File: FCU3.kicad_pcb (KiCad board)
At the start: 4 copper layers, 36.7 x 36.7 mm, 93 parts, among them J1 SM06B-SRSS-TB_LF__SN_, J2 SM06B-SRSS-TB_LF__SN_, J3 UJ20-C-H-G-SMT-1-P16-TR, J4 SM08B-SRSS-TB_LF__SN_, J6 UJ20-C-H-G-SMT-1-P16-TR, Q2 SS8050, U1 MPU-6500, U2 NCV4274AST33T3G, U3 MCP1700x-330xxTT, U5 STM32F405RGTx, Y1 LFXTAL055207Bulk

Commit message: Layout Draft Complete
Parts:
- removed the C1 at (220.5, 81.2)
- removed the C1 at (140.7, 81.2)
- removed C10: 10uF, Capacitor_SMD:C_0603_1608Metric_Pad1.08x0.95mm_HandSolder
- removed the C11 at (212.4, 92.3)
- removed the C11 at (155.6, 90.0)
- removed C12, C13, C14, C4, C5, C6: 100nF, Capacitor_SMD:C_0603_1608Metric_Pad1.08x0.95mm_HandSolder
- removed C15, C16: 27pF, Capacitor_SMD:C_0603_1608Metric_Pad1.08x0.95mm_HandSolder
- removed the C18 at (219.6, 97.9)
- removed the C18 at (155.6, 91.6)
- removed the C19 at (212.4, 95.7)
- removed the C19 at (141.1, 85.4)
- removed the C20 at (220.5, 84.6)
- removed the C20 at (143.4, 85.4)
- removed the C21 at (212.4, 99.0)
- removed the C21 at (145.8, 85.4)
- removed the C22 at (202.8, 102.9)
- removed the C22 at (148.2, 85.4)
- removed the C23 at (202.8, 104.9)
- removed the C23 at (150.7, 85.4)
- removed C32, C33: 27pF, Capacitor_SMD:C_0603_1608Metric
- removed C7, C8, C9: 2.2uF, Capacitor_SMD:C_0603_1608Metric_Pad1.08x0.95mm_HandSolder
- removed the D1 at (137.7, 82.3)
- removed the D1 at (213.7, 81.8)
- removed the H1 at (132.4, 74.5)
- removed the H1 at (188.7, 74.9)
- removed the H2 at (188.7, 82.0)
- removed the H2 at (162.9, 74.5)
- removed the H3 at (188.7, 89.2)
- removed the H3 at (162.9, 105.0)
- removed the H4 at (132.4, 105.0)
- removed the H4 at (188.7, 96.3)
- removed J2: SM06B-SRSS-TB_LF__SN_, KSE_connector:JST_SM06B-SRSS-TB_LF__SN_
- removed J6: UJ20-C-H-G-SMT-1-P16-TR, KSE_connector:SAMESKY_UJ20-C-H-G-SMT-1-P16-TR
- removed the JP3 at (197.3, 83.1)
- removed the JP3 at (149.9, 105.5)
- removed the PS1 at (218.5, 93.9)
- removed the PS1 at (154.2, 86.5)
- removed Q2: SS8050, Package_TO_SOT_SMD:SOT-23
- removed R10: 4.7k, Resistor_SMD:R_0603_1608Metric_Pad0.98x0.95mm_HandSolder
- removed the R11 at (193.7, 82.3)
- removed the R11 at (150.1, 88.6)
- removed R15, R9: 5.1k, Resistor_SMD:R_0805_2012Metric_Pad1.20x1.40mm_HandSolder
- removed the R5 at (216.7, 97.9)
- removed the R5 at (152.8, 90.9)
- removed the R6 at (216.7, 99.9)
- removed the R6 at (150.1, 90.2)
- removed the R8 at (190.5, 108.8)
- removed the R8 at (155.1, 72.2)
- removed the U1 at (198.8, 104.6)
- removed the U1 at (160.8, 98.7)
- removed U5: STM32F405RGTx, Package_QFP:LQFP-64_10x10mm_P0.5mm
- added C1: 1uF, Capacitor_SMD:C_0402_1005Metric, F.Cu at (154.3, 68.6)
- added C11: 22uF, Capacitor_SMD:C_1206_3216Metric, F.Cu at (164.2, 90.5)
- added C18: 100nF, Capacitor_SMD:C_0402_1005Metric, F.Cu at (162.6, 89.4)
- added C19: 22uF, Capacitor_SMD:C_1206_3216Metric, F.Cu at (158.1, 83.9)
- added C20: 1uF, Capacitor_SMD:C_0402_1005Metric, F.Cu at (154.3, 71.7)
- added C21: 22uF, Capacitor_SMD:C_1206_3216Metric, F.Cu at (158.1, 86.3)
- added C22: 100nF, Capacitor_SMD:C_0402_1005Metric, F.Cu at (147.4, 81.5)
- added C23: 100nF, Capacitor_SMD:C_0402_1005Metric, F.Cu at (151.2, 84.9)
- added D1: SS14-M3/5AT, Diode_SMD:D_SMA, F.Cu at (148.4, 70.6)
- added D4: LED Green, Diode_SMD:D_0603_1608Metric, F.Cu at (147.8, 102.1)
- added H1: MountingHole_Pad_MP, MountingHole:MountingHole_3.2mm_M3_DIN965_Pad, F.Cu at (132.8, 70.1)
- added H2: MountingHole_Pad_MP, MountingHole:MountingHole_3.2mm_M3_DIN965_Pad, F.Cu at (162.4, 70.0)
- added H3: MountingHole_Pad_MP, MountingHole:MountingHole_3.2mm_M3_DIN965_Pad, F.Cu at (131.9, 100.5)
- added H4: MountingHole_Pad_MP, MountingHole:MountingHole_3.2mm_M3_DIN965_Pad, F.Cu at (162.4, 100.5)
- added J5: SM06B-SRSS-TB(LF)(SN), KSE_connector:JST_SM06B-SRSS-TB(LF)(SN), F.Cu at (160.4, 78.0)
- added JP3: SolderJumper_2_Bridged, Jumper:SolderJumper-2_P1.3mm_Bridged2Bar_Pad1.0x1.5mm, B.Cu at (143.1, 102.4)
- added PS1: TPSM84338RCJR, KSE_DCDC:TPSM84338RCJR, F.Cu at (159.2, 89.7)
- added Q1: SS8050, Package_TO_SOT_SMD:SOT-23, F.Cu at (156.9, 96.2)
- added R11: 10k, Resistor_SMD:R_0402_1005Metric, F.Cu at (158.4, 94.6)
- added R5: 10k, Resistor_SMD:R_0402_1005Metric, F.Cu at (162.6, 87.4)
- added R6: 140k, Resistor_SMD:R_0402_1005Metric, F.Cu at (160.9, 86.5)
- added R8: 10k, Resistor_SMD:R_0402_1005Metric, F.Cu at (154.2, 98.2)
- added U1: MPU-6500, KSE_sensor:QFN40P300X300X95-25N, F.Cu at (147.3, 84.2)
- C17: footprint Capacitor_SMD:C_0603_1608Metric_Pad1.08x0.95mm_HandSolder -> Capacitor_SMD:C_0402_1005Metric
- C2: value 1uF -> 18pF; footprint Capacitor_SMD:C_0603_1608Metric_Pad1.08x0.95mm_HandSolder -> Capacitor_SMD:C_0603_1608Metric; moved to F.Cu
- C3: value 100nF -> 18pF; footprint Capacitor_SMD:C_0603_1608Metric_Pad1.08x0.95mm_HandSolder -> Capacitor_SMD:C_0603_1608Metric
- D2: value SS14 -> LED Red; footprint Diode_SMD:D_SMA -> Diode_SMD:D_0603_1608Metric
- J1: value SM06B-SRSS-TB_LF__SN_ -> SM06B-SRSS-TB(LF)(SN); footprint KSE_connector:JST_SM06B-SRSS-TB_LF__SN_ -> KSE_connector:JST_SM06B-SRSS-TB(LF)(SN)
- J4: value SM08B-SRSS-TB_LF__SN_ -> SM08B-SRSS-TB(LF)(SN); footprint KSE_connector:JST_SM08B-SRSS-TB_LF__SN_ -> KSE_connector:JST_SM08B-SRSS-TB(LF)(SN)
- R1: value 75k -> 4.7k; footprint Resistor_SMD:R_0603_1608Metric_Pad0.98x0.95mm_HandSolder -> Resistor_SMD:R_0402_1005Metric; moved to F.Cu
- R2, R3: value 10k -> 4.7k; footprint Resistor_SMD:R_0603_1608Metric_Pad0.98x0.95mm_HandSolder -> Resistor_SMD:R_0402_1005Metric; moved to F.Cu
- R4: value 1k -> 680; footprint Resistor_SMD:R_0603_1608Metric_Pad0.98x0.95mm_HandSolder -> Resistor_SMD:R_0402_1005Metric; moved to F.Cu
- R7: value 4.7k -> 680; footprint Resistor_SMD:R_0603_1608Metric_Pad0.98x0.95mm_HandSolder -> Resistor_SMD:R_0402_1005Metric; moved to F.Cu
- S1: value TS32-7-35-BK-B-260-RA-SMT-TR -> NO
- U2: value NCV4274AST33T3G -> AP7375-33SA-7; footprint KSE_DCDC:SOT230P700X175-4N -> KSE_DCDC:AP7375-33SA-7_DIO
- U3: value MCP1700x-330xxTT -> STM32F405RGT6; footprint Package_TO_SOT_SMD:SOT-23 -> Package_QFP:LQFP-64_10x10mm_P0.5mm; moved to F.Cu
- Y1: value LFXTAL055207Bulk -> 12MHz; footprint KSE_passive:Crystal_HC49-4H_Vertical -> KSE_passive:Crystal_SMD_Abracon_ABM8AIG-4Pin_3.2x2.5mm; moved to F.Cu
- moved R17 63.1 mm to (132.5, 74.5)
- moved R16 62.4 mm to (132.5, 75.6)
- moved D3 58.6 mm to (157.2, 70.6), turned to -90 degrees
- moved R14 58.3 mm to (135.8, 79.8)
- moved J3 58.3 mm to (141.2, 66.8), turned to 180 degrees
- moved R13 56.2 mm to (137.7, 79.8)
- moved C34 55.4 mm to (137.5, 98.7), turned to -90 degrees
- moved R12 55.1 mm to (163.7, 87.1), turned to -90 degrees
- moved C29 53.8 mm to (139.6, 86.3), turned to 180 degrees
- moved C27 53.6 mm to (136.1, 97.0), turned to 90 degrees
- moved C26 52.0 mm to (138.2, 87.7), turned to 180 degrees
- moved U2 51.8 mm to (152.8, 70.1), turned to -90 degrees
- moved C31 47.0 mm to (145.3, 101.7), turned to 180 degrees
- moved C28 44.2 mm to (145.3, 100.7), turned to 180 degrees
- moved C30 43.7 mm to (150.6, 89.8), turned to 90 degrees
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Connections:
- C2 pad 1: +3V3 -> /Project Architecture/Microcontroller/CLK_OUT
- C29 pad 1: Net-(U5-VCAP_2) -> Net-(U3-VCAP_2)
- C30 pad 1: Net-(U5-VCAP_1) -> Net-(U3-VCAP_1)
- D2 pad 1: Net-(D1-K) -> DGND
- D2 pad 2: /(lib_symbols/V_USB -> Net-(D2-A)
- D3 pad 2: /Project Architecture/Power/10–26V to 9V2A Step-Down Converter/+9V -> +9V
- J1 pad 1: +9V -> /Project Architecture/UART5_RX
- J1 pad 2: PGND -> /Project Architecture/UART5_TX
- J1 pad 3: /Project Architecture/UART4_TX -> DGND
- J1 pad 4: /Project Architecture/UART4_RX -> +3V3
- J1 pad 5: DGND -> /Project Architecture/I2C1_SCL
- J1 pad 6: /Project Architecture/SBUS_TX -> /Project Architecture/I2C1_SDA
- J4 pad 3: /(lib_symbols/ESC_SIG_M1 -> /Project Architecture/ESC_SIG_M1
- J4 pad 4: /(lib_symbols/ESC_SIG_M2 -> /Project Architecture/ESC_SIG_M2
- J4 pad 5: /(lib_symbols/ESC_SIG_M4 -> /Project Architecture/ESC_SIG_M4
- J4 pad 6: /(lib_symbols/ESC_SIG_M3 -> /Project Architecture/ESC_SIG_M3
- J4 pad 7: /(lib_symbols/ANA_ADC_CURR -> /Project Architecture/ANA_ADC_CURR
- J4 pad 8: /(lib_symbols/UART1_RX -> /Project Architecture/UART1_RX
- R1 pad 1: /(lib_symbols/ANA_ADC_VBAT -> +3V3
- R1 pad 2: +VBAT -> /Project Architecture/I2C1_SDA
- R2 pad 1: AGND -> +3V3
- R2 pad 2: /(lib_symbols/ANA_ADC_VBAT -> /Project Architecture/I2C1_SCL
- R3 pad 1: +3V3 -> /Project Architecture/SBUS_TX
- R3 pad 2: /(lib_symbols/UART2_RX -> Net-(Q1-B)
- R4 pad 1: Net-(Q2-B) -> /Project Architecture/Microcontroller/LED1
- R4 pad 2: /Project Architecture/SBUS_TX -> Net-(D2-A)
- R7 pad 1: /Project Architecture/I2C1_SCL -> /Project Architecture/Microcontroller/LED0
- R7 pad 2: +3V3 -> Net-(D4-A)
- S1 pad 1: /Project Architecture/Microcontroller/DFU_Enable -> +3V3
- S1 pad 2: +3V3 -> /Project Architecture/Microcontroller/DFU_Enable
- S1 pad SH1: (no net) -> DGND
- S1 pad SH2: (no net) -> DGND
- U2 pad 2: DGND -> +3V3
- U2 pad 3: +3V3 -> DGND
- U3 pad 1: DGND -> unconnected-(U3-VBAT-Pad1)
- U3 pad 2: +3V3 -> unconnected-(U3-PC13-Pad2)
- U3 pad 3: Net-(D1-K) -> unconnected-(U3-PC14-Pad3)
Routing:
- net +3V3: track 147.8 -> 72.0 mm, vias 11 -> 13
- net PGND: track 92.4 -> 41.5 mm, vias 11 -> 8
- net /(lib_symbols/Microcontroller/DFU_Enable: track 41.9 -> 0.00 mm, vias 4 -> 0
- net /(lib_symbols/UART2_RX: track 32.1 -> 0.00 mm, vias 3 -> 0
- net /Project Architecture/I2C1_SDA: track 41.2 -> 10.1 mm, vias 3 -> 2
- net /Project Architecture/I2C1_SCL: track 38.2 -> 8.11 mm, vias 4 -> 0
- net /Project Architecture/ANA_ADC_VBAT: track 0.00 -> 26.2 mm, vias 0 -> 2
- net +9V: track 54.1 -> 27.9 mm, vias 12 -> 1
- net /(lib_symbols/ANA_ADC_VBAT: track 26.0 -> 0.00 mm, vias 1 -> 0
- net /Project Architecture/ANA_ADC_CURR: track 0.00 -> 25.0 mm, vias 0 -> 2
- net /Project Architecture/UART5_TX: track 27.4 -> 4.21 mm, vias 3 -> 0
- net /Project Architecture/ESC_SIG_M1: track 0.00 -> 22.5 mm, vias 0 -> 2
- net /Project Architecture/Microcontroller/DFU_Enable: track 0.00 -> 22.3 mm
- net /(lib_symbols/ESC_SIG_M3: track 22.1 -> 0.00 mm, vias 2 -> 0
- net /Project Architecture/SBUS_TX: track 5.49 -> 27.2 mm, vias 1 -> 2
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- added copper zone on In2.Cu, net +3V3
- added copper zone on In1.Cu, net PGND
- removed copper zone on B.Cu, net +9V
- removed copper zone on In2.Cu, net +9V
- removed copper zone on B.Cu, net PGND
- removed copper zone on In2.Cu, net PGND
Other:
- board size 36.7 x 36.7 mm -> 37 x 37 mm
- board text added: "9V to 3.3V LDO Layout"
- board text added: "IMU Layout"
- board text added: "MCU Layout"
- board text added: "SBUS Inverter Layout"

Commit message: DRC/ERC Remaining
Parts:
- added J2: ST-LINK_Header, Connector_PinHeader_1.27mm:PinHeader_2x03_P1.27mm_Vertical_SMD, B.Cu at (148.7, 71.8)
- moved R3 3.01 mm to (154.0, 94.9)
- moved R11 3.01 mm to (155.5, 95.6)
- moved Q1 3.01 mm to (154.1, 97.1)
- moved R8 2.55 mm to (151.6, 98.2)
- moved R13 2.24 mm to (135.8, 78.8), turned to 180 degrees
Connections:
- R4 pad 1: /Project Architecture/Microcontroller/LED1 -> /Project Architecture/LED1
- R7 pad 1: /Project Architecture/Microcontroller/LED0 -> /Project Architecture/LED0
- U3 pad 46: /Project Architecture/Microcontroller/LED0 -> /Project Architecture/Microcontroller/SWDIO
- U3 pad 49: /Project Architecture/Microcontroller/LED1 -> /Project Architecture/Microcontroller/SWCLK
- U3 pad 55: unconnected-(U3-PB3-Pad55) -> /Project Architecture/Microcontroller/SWO
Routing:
- net /Project Architecture/Microcontroller/SWO: track 0.00 -> 31.2 mm, vias 0 -> 3
- net /Project Architecture/Microcontroller/SWDIO: track 0.00 -> 30.0 mm, vias 0 -> 3
- net /Project Architecture/Microcontroller/SWCLK: track 0.00 -> 25.9 mm, vias 0 -> 2
- net /Project Architecture/DIG_IMU_EXTI: track 1.80 -> 17.5 mm
- net /Project Architecture/SPI1_SCK: track 20.6 -> 33.8 mm, vias 2 -> 3
- net +9V: track 27.9 -> 40.5 mm
- net /Project Architecture/DIG_IMU_CS: track 5.87 -> 18.4 mm
- net +3V3: track 72.0 -> 83.5 mm, vias 13 -> 14
- net /Project Architecture/SPI1_SDO: track 3.16 -> 12.1 mm
- net AGND: track 34.1 -> 38.6 mm
- net DGND: track 80.6 -> 85.0 mm, vias 21 -> 22
- net /Project Architecture/SBUS_TX: track 27.2 -> 30.1 mm
- net /Project Architecture/UART4_RX: track 32.6 -> 35.2 mm
- net /Project Architecture/Microcontroller/LED1: track 2.25 -> 0.00 mm, vias 2 -> 0
- net /Project Architecture/UART2_RX: track 13.5 -> 11.4 mm
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- added copper zone on B.Cu, net +9V

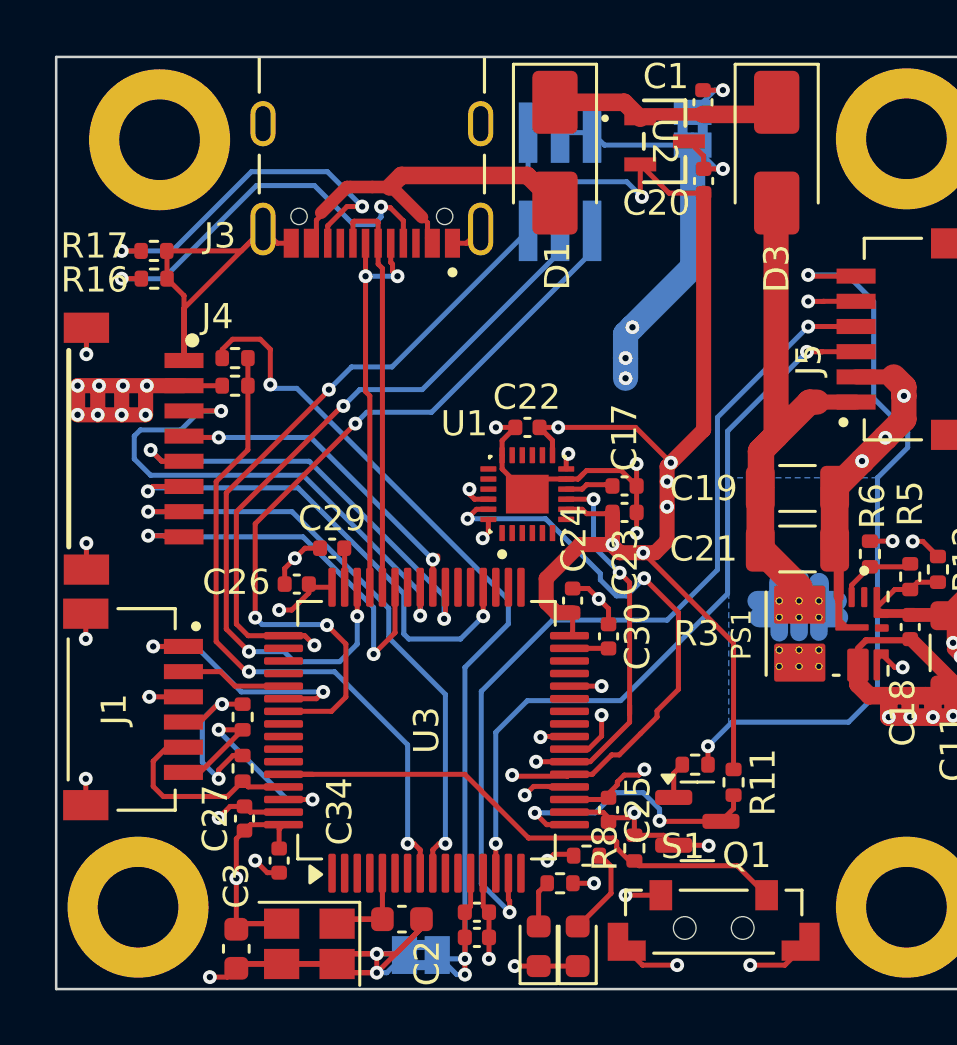
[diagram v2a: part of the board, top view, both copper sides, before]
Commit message: Added debugger pads, needs to fix LED
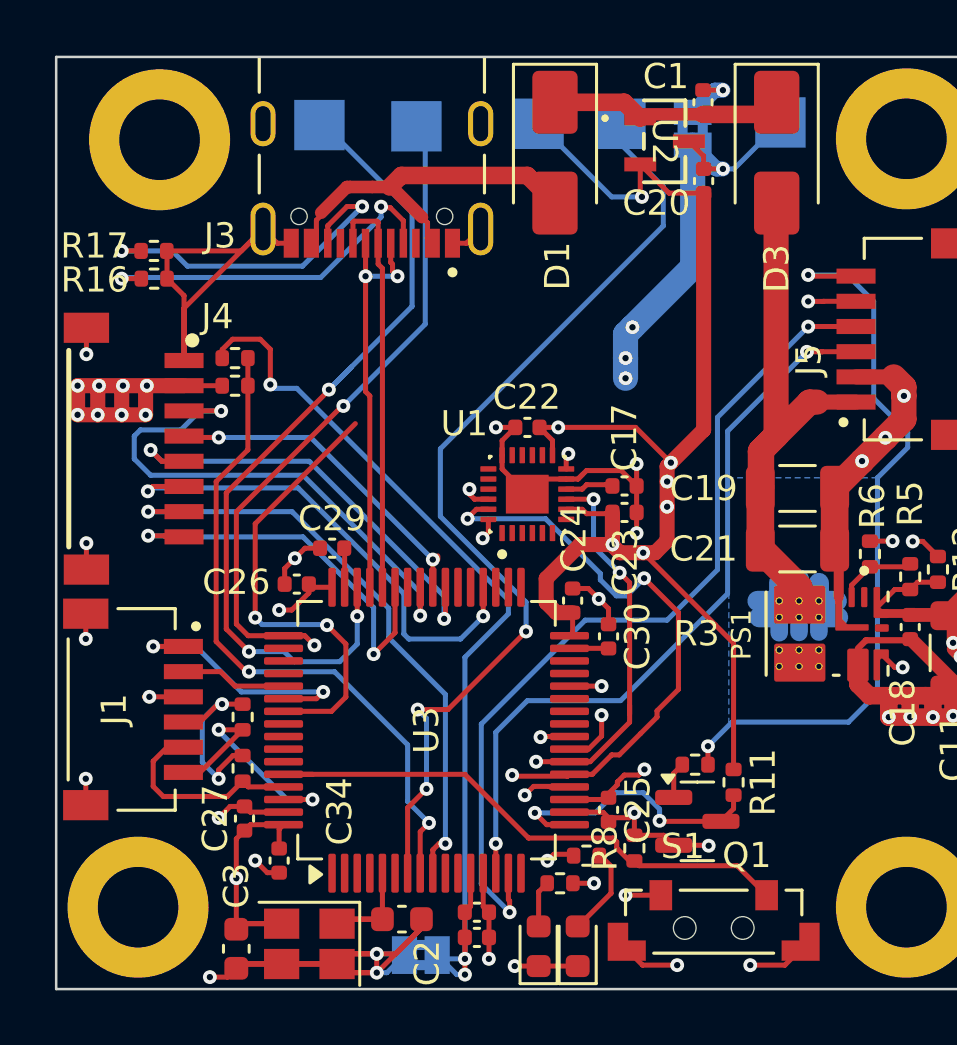
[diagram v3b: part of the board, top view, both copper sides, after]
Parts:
- removed J2: ST-LINK_Header, Connector_PinHeader_1.27mm:PinHeader_2x03_P1.27mm_Vertical_SMD
- added TP1: VCC, TestPoint:TestPoint_Pad_2.0x2.0mm, B.Cu at (147.8, 69.5)
- added TP2: SWDIO, TestPoint:TestPoint_Pad_2.0x2.0mm, B.Cu at (139.1, 69.5)
- added TP3: SWCLK, TestPoint:TestPoint_Pad_2.0x2.0mm, B.Cu at (142.9, 69.5)
- added TP4: GND, TestPoint:TestPoint_Pad_2.0x2.0mm, B.Cu at (157.4, 69.4)
- added TP5: RESET, TestPoint:TestPoint_Pad_2.0x2.0mm, B.Cu at (151.1, 69.5)
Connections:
- U3 pad 55: /Project Architecture/Microcontroller/SWO -> unconnected-(U3-PB3-Pad55)
- U3 pad 7: unconnected-(U3-NRST-Pad7) -> Net-(U3-NRST)
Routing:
- net Net-(U3-NRST): track 0.00 -> 38.5 mm, vias 0 -> 3
- net /Project Architecture/Microcontroller/SWO: track 31.2 -> 0.00 mm, vias 3 -> 0
- net unconnected-(U3-PB3-Pad55): track 0.00 -> 18.2 mm, vias 0 -> 2
- net /Project Architecture/Microcontroller/SWDIO: track 30.0 -> 34.3 mm
- net DGND: track 85.0 -> 82.6 mm
- net /Project Architecture/USB_CC1: track 16.0 -> 14.7 mm
- net +3V3: track 83.5 -> 82.3 mm
- net /Project Architecture/Microcontroller/SWCLK: track 25.9 -> 26.8 mm
- net /Project Architecture/UART4_RX: track 35.2 -> 34.5 mm
- net /Project Architecture/USB_CC2: track 14.7 -> 14.0 mm
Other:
- board text added: "CLK"
- board text added: "DIO"
- board text added: "GND"
- board text added: "RST"
- board text added: "VCC"

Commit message: Finished DRC/ERC
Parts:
- moved R7 7.97 mm to (151.1, 92.0), turned to 0 degrees
- moved R4 5.61 mm to (151.1, 93.0)
- moved D4 1.65 mm to (149.4, 102.1)
- moved D2 1.60 mm to (147.8, 102.1)
- moved H1 0.75 mm to (132.0, 70.1)
- moved R6 0.53 mm to (160.9, 86.0)
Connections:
- C11 pad 1: /Project Architecture/Power/VBAT -> +VBAT
- C18 pad 1: /Project Architecture/Power/VBAT -> +VBAT
- J1 pad MP: (no net) -> PGND
- J4 pad MP: (no net) -> PGND
- J5 pad MP: (no net) -> PGND
- PS1 pad 6: /Project Architecture/Power/VBAT -> +VBAT
- R4 pad 1: /Project Architecture/LED1 -> /Project Architecture/Microcontroller/LED1
- R7 pad 1: /Project Architecture/LED0 -> /Project Architecture/Microcontroller/LED0
- U3 pad 26: unconnected-(U3-PB0-Pad26) -> /Project Architecture/Microcontroller/LED1
- U3 pad 27: unconnected-(U3-PB1-Pad27) -> /Project Architecture/Microcontroller/LED0
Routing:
- net PGND: track 41.5 -> 75.7 mm, vias 8 -> 12
- net unconnected-(U3-PB3-Pad55): track 18.2 -> 0.00 mm, vias 2 -> 0
- net /Project Architecture/Power/VBAT: track 16.5 -> 0.00 mm, vias 4 -> 0
- net +VBAT: track 13.3 -> 26.9 mm, vias 8 -> 10
- net Net-(D4-A): track 1.85 -> 13.5 mm, vias 0 -> 2
- net Net-(D2-A): track 3.65 -> 13.1 mm, vias 0 -> 2
- net (no net): track 4.15 -> 0.00 mm, vias 4 -> 0
- net /Project Architecture/DIG_IMU_EXTI: track 17.5 -> 13.5 mm
- net /Project Architecture/SPI1_SDI: track 15.2 -> 17.8 mm, vias 3 -> 2
- net /Project Architecture/Microcontroller/LED1: track 0.00 -> 1.63 mm
- net /Project Architecture/Microcontroller/LED0: track 0.00 -> 1.63 mm
- net /Project Architecture/SPI1_SCK: track 33.8 -> 35.4 mm
- net /Project Architecture/Microcontroller/SWCLK: track 26.8 -> 25.5 mm, vias 2 -> 1
- net +9V: track 40.5 -> 39.2 mm
- net /Project Architecture/Microcontroller/SWDIO: track 34.3 -> 33.0 mm
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
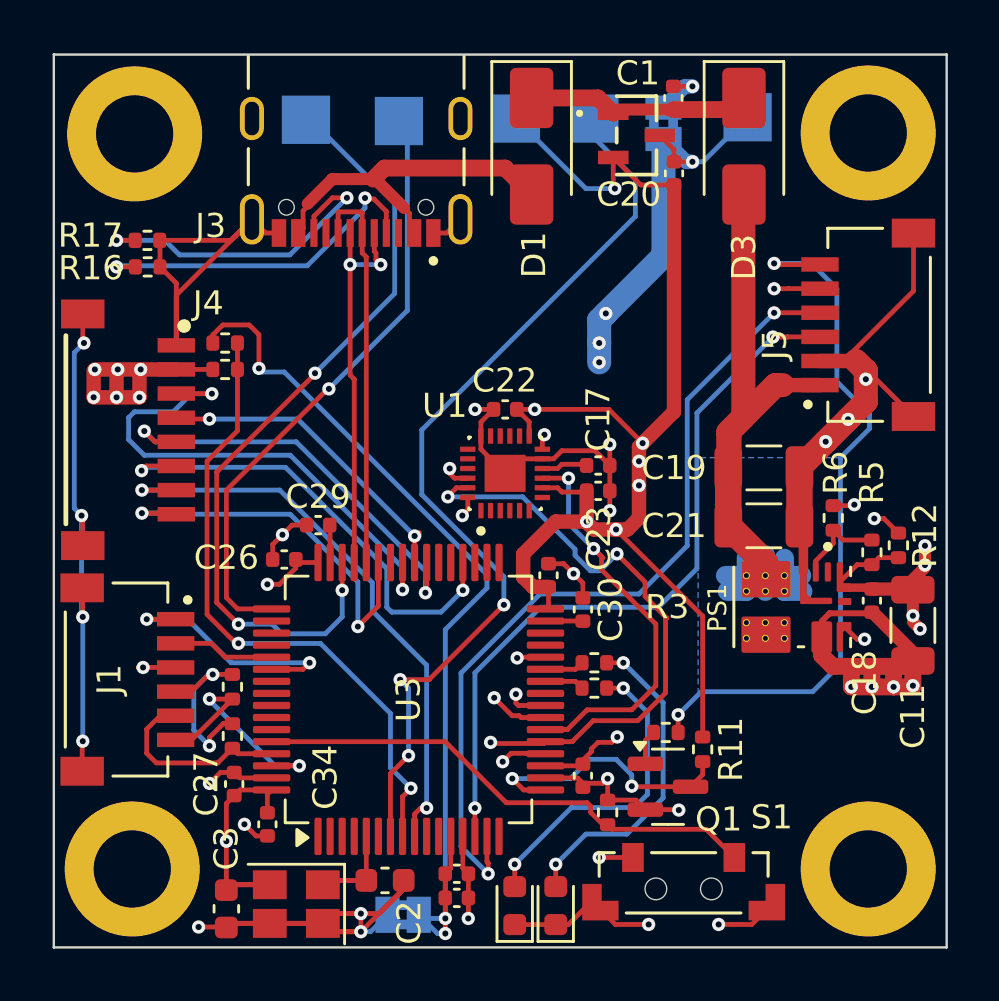
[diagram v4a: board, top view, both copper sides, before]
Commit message: Fixed ESC connector pinout
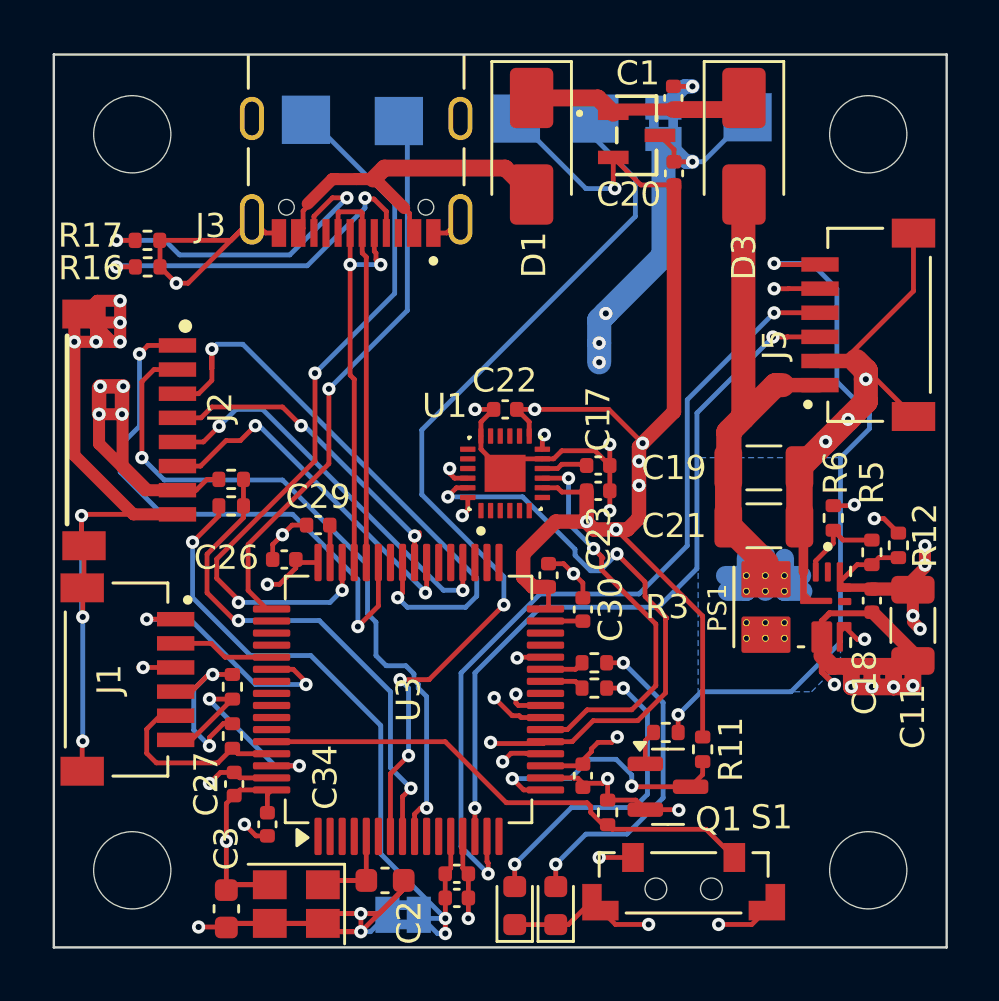
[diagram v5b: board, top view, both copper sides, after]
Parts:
- removed J4: SM08B-SRSS-TB(LF)(SN), KSE_connector:JST_SM08B-SRSS-TB(LF)(SN)
- added J2: SM08B-SRSS-TB(LF)(SN), KSE_connector:JST_SM08B-SRSS-TB(LF)(SN), F.Cu at (129.0, 82.3)
- H1, H2, H3, H4: value MountingHole_Pad_MP -> MountingHole; footprint MountingHole:MountingHole_3.2mm_M3_DIN965_Pad -> MountingHole:MountingHole_3.2mm_M3_ISO7380
- moved R13 6.75 mm to (136.0, 85.5)
- moved R14 4.56 mm to (136.0, 84.4)
- moved H1 0.10 mm to (131.9, 70.1)
- moved H2 0.05 mm to (162.4, 70.1)
- moved H3 0.05 mm to (131.9, 100.6)
- moved H4 0.05 mm to (162.4, 100.6)
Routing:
- net +VBAT: track 26.9 -> 54.1 mm, vias 10 -> 9
- net PGND: track 75.7 -> 89.7 mm, vias 12 -> 17
- net AGND: track 38.6 -> 30.1 mm
- net /Project Architecture/UART1_RX: track 16.4 -> 23.6 mm
- net /Project Architecture/ANA_ADC_VBAT: track 27.4 -> 21.8 mm
- net /Project Architecture/ANA_ADC_CURR: track 25.1 -> 29.8 mm
- net /Project Architecture/ESC_SIG_M3: track 19.8 -> 16.7 mm
- net /Project Architecture/ESC_SIG_M1: track 22.0 -> 24.8 mm
- net /Project Architecture/ESC_SIG_M4: track 17.8 -> 15.1 mm
- net /Project Architecture/Microcontroller/SWDIO: track 33.0 -> 30.7 mm
- net /Project Architecture/Microcontroller/SWCLK: track 25.5 -> 24.0 mm
- net /Project Architecture/SBUS_TX: track 30.1 -> 29.5 mm
